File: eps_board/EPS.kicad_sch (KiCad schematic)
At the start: 23 parts

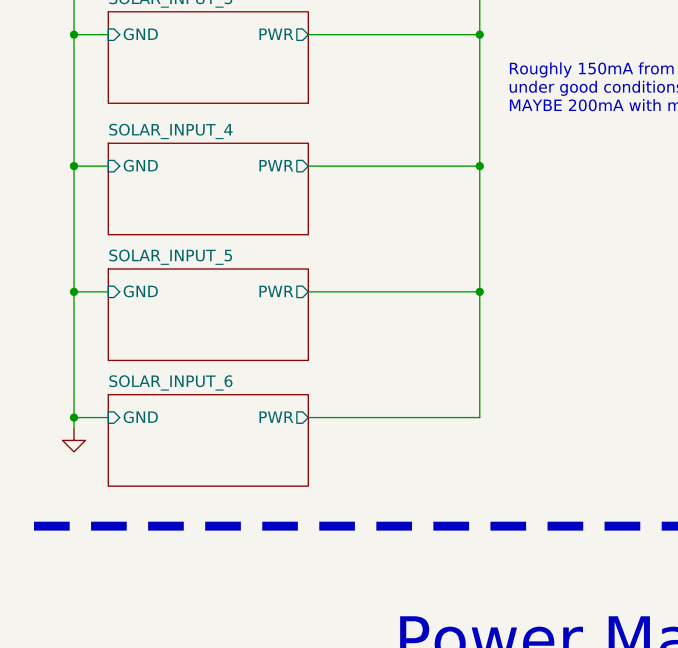
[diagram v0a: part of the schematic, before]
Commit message: EPS use M50 2x3 connectors for solar cells. remove 2 connectors since they are all tied together and top/bottom can be routed through sides and side connectors
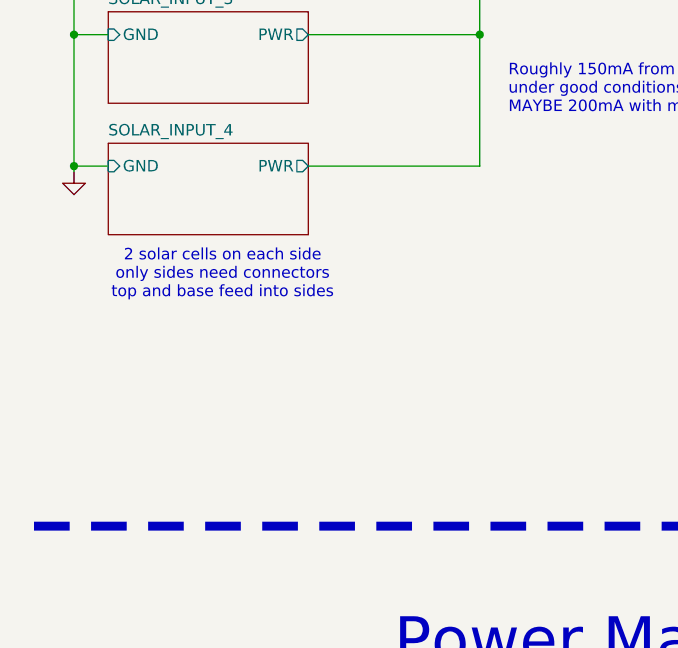
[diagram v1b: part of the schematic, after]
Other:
- removed sheet SOLAR_INPUT_5
- removed sheet SOLAR_INPUT_6
- note added: "2 solar cells on each side only sides need connectors top and base feed into sides"
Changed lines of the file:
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@@
 	)
 	(junction
-		(at 16.51 94.615)
-		(diameter 0)
-		(color 0 0 0 0)
-	)
-	(junction
 		(at 57.15 200.025)
 		(diameter 0)
@@
 	)
 	(junction
-		(at 16.51 80.645)
-		(diameter 0)
-		(color 0 0 0 0)
-	)
-	(junction
 		(at 94.615 33.02)
 		(diameter 0)
@@
 	)
 	(junction
-		(at 61.595 66.675)
-		(diameter 0)
-		(color 0 0 0 0)
-	)
-	(junction
 		(at 233.045 153.67)
 		(diameter 0)
@@
 	)
 	(junction
-		(at 61.595 80.645)
-		(diameter 0)
-		(color 0 0 0 0)
-	)
-	(junction
 		(at 384.81 170.815)
 		(diameter 0)
@@
 	(wire
 		(pts
-			(xy 16.51 66.675) (xy 16.51 80.645)
+			(xy 16.51 66.675) (xy 16.51 67.31)
 		)
 		(stroke
@@
 	(wire
 		(pts
-			(xy 42.545 80.645) (xy 61.595 80.645)
-		)
-		(stroke
-			(width 0)
-			(type default)
-		)
-	)
-	(wire
-		(pts
 			(xy 233.045 153.67) (xy 233.045 154.305)
 		)
@@
 	(wire
 		(pts
-			(xy 61.595 80.645) (xy 61.595 94.615)
-		)
-		(stroke
-			(width 0)
-			(type default)
-		)
-	)
-	(wire
-		(pts
 			(xy 88.265 245.11) (xy 92.71 245.11)
 		)
@@
 	(wire
 		(pts
-			(xy 16.51 94.615) (xy 20.32 94.615)
-		)
-		(stroke
-			(width 0)
-			(type default)
-		)
-	)
-	(wire
-		(pts
 			(xy 128.27 220.345) (xy 124.46 220.345)
 		)
@@
 	(wire
 		(pts
-			(xy 42.545 94.615) (xy 61.595 94.615)
-		)
-		(stroke
-			(width 0)
-			(type default)
-		)
-	)
-	(wire
-		(pts
 			(xy 128.27 217.17) (xy 124.46 217.17)
 		)
@@
 	(wire
 		(pts
-			(xy 16.51 80.645) (xy 16.51 94.615)
-		)
-		(stroke
-			(width 0)
-			(type default)
-		)
-	)
-	(wire
-		(pts
 			(xy 53.975 240.665) (xy 52.07 240.665)
 		)
@@
 	(wire
 		(pts
-			(xy 16.51 80.645) (xy 20.32 80.645)
-		)
-		(stroke
-			(width 0)
-			(type default)
-		)
-	)
-	(wire
-		(pts
 			(xy 400.685 70.485) (xy 400.685 69.85)
 		)
@@
 	(wire
 		(pts
-			(xy 16.51 94.615) (xy 16.51 95.885)
-		)
-		(stroke
-			(width 0)
-			(type default)
-		)
-	)
-	(wire
-		(pts
 			(xy 88.265 240.665) (xy 92.71 240.665)
 		)
@@
 	(wire
 		(pts
-			(xy 61.595 66.675) (xy 61.595 80.645)
-		)
-		(stroke
-			(width 0)
-			(type default)
-		)
-	)
-	(wire
-		(pts
 			(xy 128.27 204.47) (xy 124.46 204.47)
 		)
@@
 		)
 	)
+	(text "2 solar cells on each side\nonly sides need connectors\ntop and base feed into sides"
+		(exclude_from_sim no)
+		(at 33.02 78.74 0)
+		(effects
+			(font
+				(size 1.27 1.27)
+			)
+		)
+	)
 	(text "Current Monitors &\nLoad switching"
 		(exclude_from_sim no)
@@
 	(symbol
 		(lib_id "EPS-rescue:GND-power")
-		(at 16.51 95.885 0)
+		(at 16.51 67.31 0)
 		(unit 1)
 		(exclude_from_sim no)
@@
 		(dnp no)
 		(property "Reference" "#PWR014"
-			(at 16.51 102.235 0)
+			(at 16.51 73.66 0)
 			(effects
 				(font
@@
 		)
 		(property "Value" "GND"
-			(at 16.637 100.2792 0)
+			(at 16.637 71.7042 0)
 			(effects
 				(font
@@
 		)
 		(property "Footprint" ""
-			(at 16.51 95.885 0)
+			(at 16.51 67.31 0)
 			(effects
 				(font
@@
 		)
 		(property "Datasheet" ""
-			(at 16.51 95.885 0)
+			(at 16.51 67.31 0)
 			(effects
 				(font
@@
 		)
 		(property "Description" ""
-			(at 16.51 95.885 0)
+			(at 16.51 67.31 0)
 			(effects
 				(font
@@
 				)
 			)
-		)
-	)
-	(sheet
-		(at 20.32 78.105)
-		(size 22.225 10.16)
-		(fields_autoplaced yes)
-		(stroke
-			(width 0)
-			(type solid)
-		)
-		(fill
-			(color 0 0 0 0.0000)
-		)
-		(property "Sheetname" "SOLAR_INPUT_5"
-			(at 20.32 77.3934 0)
-			(effects
-				(font
-					(size 1.27 1.27)
-				)
-				(justify left bottom)
-			)
-		)
-		(property "Sheetfile" "SOLAR_INPUT.kicad_sch"
-			(at 20.32 88.8496 0)
-			(effects
-				(font
-					(size 1.27 1.27)
-				)
-				(justify left top)
-				(hide yes)
-			)
-		)
-		(pin "PWR" output
-			(at 42.545 80.645 0)
-			(effects
-				(font
-					(size 1.27 1.27)
-				)
-				(justify right)
-			)
-		)
-		(pin "GND" input
-			(at 20.32 80.645 180)
-			(effects
-				(font
-					(size 1.27 1.27)
-				)
-				(justify left)
-			)
-		)
-		(instances
-			(project "EPS"
-				(path "/05170af6-30ef-4c3a-b972-f098085da1bc"
-					(page "6")
-				)
-			)
-		)
-	)
-	(sheet
-		(at 20.32 92.075)
-		(size 22.225 10.16)
-		(fields_autoplaced yes)
-		(stroke
-			(width 0)
-			(type solid)
-		)
-		(fill
-			(color 0 0 0 0.0000)
-		)
-		(property "Sheetname" "SOLAR_INPUT_6"
-			(at 20.32 91.3634 0)
-			(effects
-				(font
-					(size 1.27 1.27)
-				)
-				(justify left bottom)
-			)
-		)
-		(property "Sheetfile" "SOLAR_INPUT.kicad_sch"
-			(at 20.32 102.8196 0)
-			(effects
-				(font
-					(size 1.27 1.27)
-				)
-				(justify left top)
-				(hide yes)
-			)
-		)
-		(pin "PWR" output
-			(at 42.545 94.615 0)
-			(effects
-				(font
-					(size 1.27 1.27)
-				)
-				(justify right)
-			)
-		)
-		(pin "GND" input
-			(at 20.32 94.615 180)
-			(effects
-				(font
-					(size 1.27 1.27)
-				)
-				(justify left)
-			)
-		)
-		(instances
-			(project "EPS"
-				(path "/05170af6-30ef-4c3a-b972-f098085da1bc"
-					(page "7")
-				)
-			)
